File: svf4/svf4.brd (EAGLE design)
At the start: 58.4 x 216.8 mm, 79 parts, among them IC1 OPA4130P, IC2 OPA2134P, Q1 BC550B, Q10 2N3906, Q2 BC550B, Q3 2N3904, Q4 2N3904, Q5 2N3904, Q6 2N3904, Q7 2N3906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

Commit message: finished the rough draft of the state variable board
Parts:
- removed Q10, Q7, Q8, Q9: 2N3906, dan:TO92
- removed Q3, Q4, Q5, Q6: 2N3904, dan:TO92
- removed SV5, SV6: (no value), dan:MA04-1
- added C4, C5, C6: 4.7u, dan:E2,5-6
- added JP1, JP2: (no value), dan:1X06
- added R32: 10k, dan:0207/2V
- added R33: 4.7k, dan:0207/2V
- added R34, R36: 1k, dan:0207/2V
- added R35: 100k, dan:0207/2V
- added U$1, U$2, U$3, U$4: 2N3904_, dan:TO92-EBC
- added U$5, U$6, U$7, U$8: 2N3906_, dan:TO92-EBC
- IC2: value OPA2134P -> OPA4130P; device dan:DIL08 -> dan:DIL14
- R20: value 220k -> 1k
- R27: value 1k -> 4.7k
- R28: value 1k -> 3.3k
- R29: value 1k -> 100k
- R3: value 100k -> 82k
- R30, R31: value 10k -> 100k
- moved R31 142.5 mm to (35.6, 11.4), turned to 270 degrees
- moved R30 141.2 mm to (30.5, 12.7), turned to 180 degrees
- moved R20 76.4 mm to (45.1, 71.8)
- moved R2 56.6 mm to (48.9, 50.2), turned to 90 degrees
- moved R27 44.1 mm to (43.2, 113.0)
- moved R28 41.7 mm to (39.4, 113.0)
- moved D2 38.2 mm to (10.8, 25.4), turned to 90 degrees
- moved R24 37.0 mm to (44.5, 19.1), turned to 180 degrees
- moved R4 36.2 mm to (47.6, 34.3), turned to 270 degrees
- moved R15 35.6 mm to (16.5, 16.5), turned to 0 degrees
- moved R3 35.4 mm to (38.7, 11.4)
- moved D1 33.9 mm to (43.2, 31.8), turned to 90 degrees
- moved R13 31.2 mm to (14.0, 27.9), turned to 270 degrees
- moved RIN1 29.2 mm to (43.8, 171.4)
- moved RIN2 29.2 mm to (14.6, 171.4)
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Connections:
- new net N$38: BPOUT.P$3, R34.2, R35.1
- new net N$41: IC2.14, R32.2, SV7.4
- new net N$42: IC2.13, R32.1, R33.2
- new net N$43: C6.-, R27.1
- new net N$44: C5.+, R26.1
- new net N$45: C4.-, R34.1
- new net N$46: JP2.4, R31.2
- new net N$47: IC2.5, R20.1
- new net N$48: IC2.6, R36.2
- net +12V: now also IC2.4; no longer IC2.8
- net -12V: now also IC2.11; no longer IC2.4
- net -1V: now also IC2.10; no longer IC2.5
- net BP: now also JP2.6; no longer SV5.1
- net GND: now also JP1.2, JP1.5, JP2.2, JP2.5, R20.2, R33.1, R35.2, U$2.B, U$4.B; no longer Q4.2, Q6.2, SV5.2, SV6.2
- net HP: now also IC2.12; no longer SV7.4
- net IN: now also IC1.2, R24.2, R30.1, R31.1, R5.2, R6.2; no longer R20.2, SV5.3
- net N$1: now also U$3.C, U$4.C; no longer Q5.3, Q6.3
- net N$10: now also U$4.E, U$8.E; no longer Q10.1, Q6.1
- net N$14: now also U$3.E, U$7.B, U$7.E, U$8.B; no longer Q10.2, Q5.1, Q9.1, Q9.2
- net N$15: now also U$3.B; no longer Q5.2
- net N$16: now also JP2.1; no longer SV5.4
- net N$17: now also U$7.C, U$8.C; no longer Q10.3, Q9.3
- net N$2: now also U$2.E, U$6.E; no longer Q4.1, Q8.1
- net N$26: now also IC2.8; no longer IC2.7
- net N$28: now also IC2.9; no longer IC2.6
- net N$3: now also U$5.C, U$6.C; no longer Q7.3, Q8.3
- net N$30: now also JP1.1; no longer SV6.4
- net N$32: now also C5.-; no longer R26.1
- net N$33: now also JP1.4; no longer R30.2
- net N$36: now also C4.+, JP1.6; no longer BPOUT.P$3, SV6.1
- net N$37: now also JP2.3, R30.2; no longer R30.1, R31.1, SV6.3
- net N$4: now also U$1.E, U$5.B, U$5.E, U$6.B; no longer Q3.1, Q7.1, Q7.2, Q8.2
- net N$40: now also JP1.3; no longer R31.2
- net N$5: now also U$1.C, U$2.C; no longer Q3.3, Q4.3
- net N$6: now also U$1.B; no longer Q3.2
- net N$7: now also IC2.7, R36.1; no longer IC1.2, R20.1, R24.2, R5.2, R6.2
- net N$8: now also C6.+; no longer R27.1
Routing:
- net +12V: track 0.00 -> 253.6 mm, vias 0 -> 5
- net -12V: track 0.00 -> 195.6 mm, vias 0 -> 5
- net BP: track 0.00 -> 187.8 mm, vias 0 -> 4
- net N$9: track 0.00 -> 151.7 mm, vias 0 -> 3
- net HP: track 0.00 -> 87.2 mm, vias 0 -> 1
- net N$30: track 0.00 -> 81.2 mm, vias 0 -> 1
- net N$33: track 0.00 -> 80.7 mm
- net N$21: track 0.00 -> 80.3 mm, vias 0 -> 3
- net LP: track 0.00 -> 78.3 mm, vias 0 -> 3
- net N$41: track 0.00 -> 72.7 mm, vias 0 -> 1
- net FCIN: track 0.00 -> 64.2 mm
- net N$6: track 0.00 -> 57.0 mm, vias 0 -> 1
- net -1V: track 0.00 -> 56.2 mm, vias 0 -> 2
- net N$25: track 0.00 -> 55.8 mm, vias 0 -> 1
- net N$31: track 0.00 -> 55.4 mm
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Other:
- board size 58.4 x 216.8 mm -> 10.6 x 2.1 mm
- board text added: "-12V"
- board text added: "BP"
- board text added: "HP"
- board text added: "In1"
- board text added: "In2"
- board text added: "LP"
- board text added: "Q1"
- board text added: "Q2"
- board text added: "Q3"
- board text added: "Q4"
- board text added: "Q5"
- board text added: "Q6"
- board text added: "Q7"
- board text added: "Q8"
- board text added: "cv"

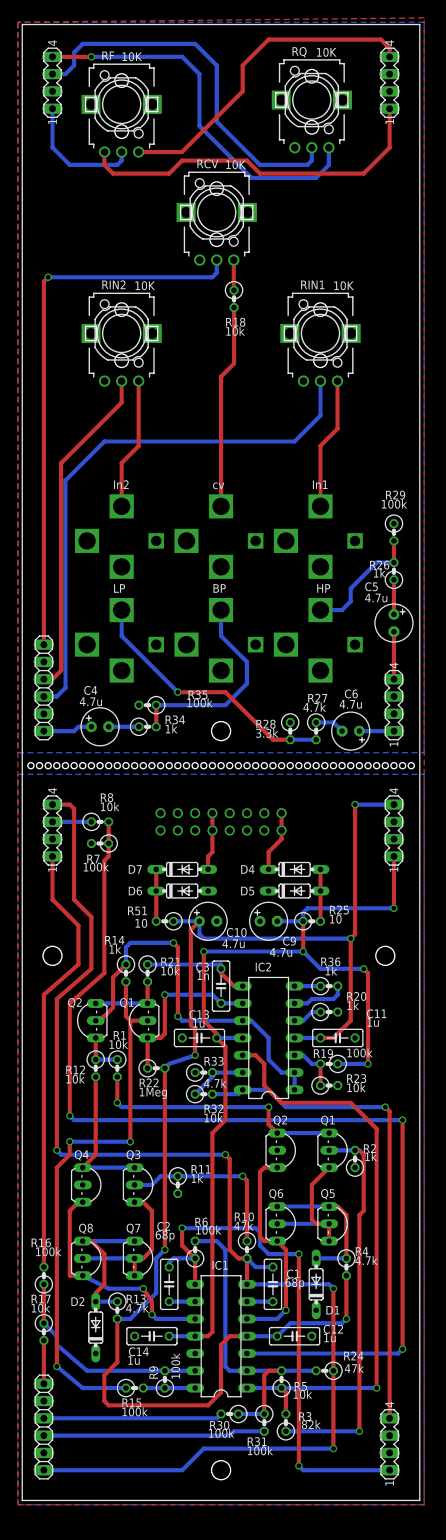
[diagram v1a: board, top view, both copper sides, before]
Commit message: fixed placement of knobs and jacks on svf
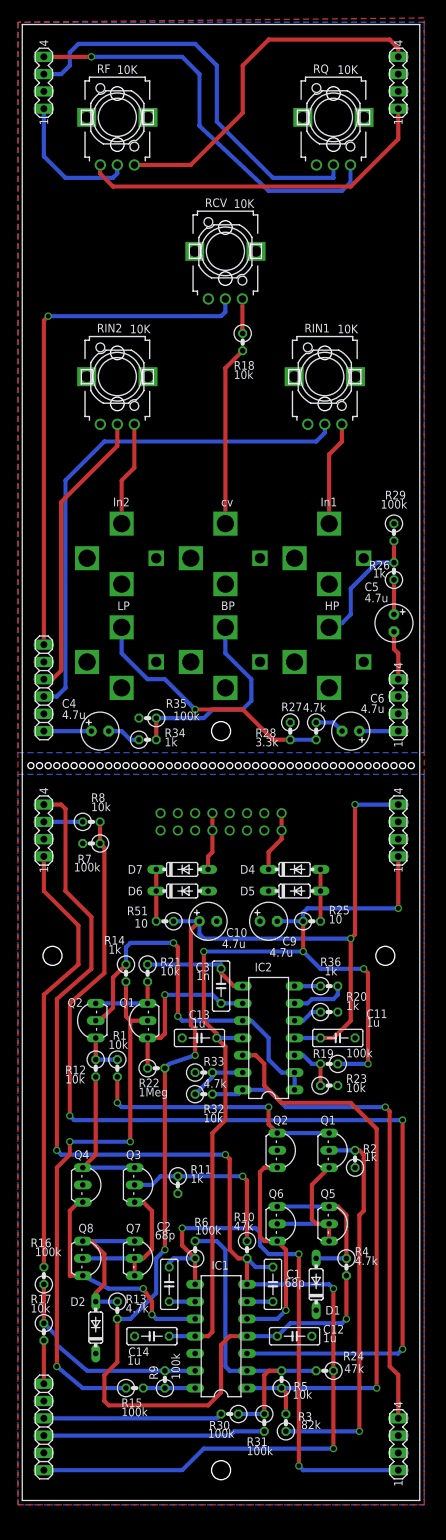
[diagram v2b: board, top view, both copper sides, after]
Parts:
- moved R18 6.48 mm to (32.4, 170.2)
- moved RIN1 6.38 mm to (44.5, 165.1)
- moved RIN2 6.38 mm to (14.0, 165.1)
- moved RCV 5.85 mm to (29.8, 183.5)
- moved RQ 4.07 mm to (45.7, 203.2)
- moved HPOUT 2.84 mm to (45.1, 123.2)
- moved IN 2.84 mm to (45.1, 138.4)
- moved BPOUT 2.62 mm to (29.8, 123.2)
- moved CVIN 2.62 mm to (29.8, 138.4)
- moved LPOUT 2.54 mm to (14.6, 123.2)
- moved IN1 2.54 mm to (14.6, 138.4)
- moved RF 2.01 mm to (14.0, 203.2)
- moved R34 1.91 mm to (18.4, 111.8)
- moved R35 1.91 mm to (18.4, 114.9)
- moved SV3 1.27 mm to (3.17, 98.4)
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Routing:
- net N$40: track 49.3 -> 42.7 mm
- net +12V: track 253.6 -> 258.8 mm
- net N$31: track 55.4 -> 60.4 mm
- net N$25: track 55.8 -> 60.6 mm
- net N$30: track 81.2 -> 76.7 mm
- net N$33: track 80.7 -> 76.4 mm
- net N$34: track 19.4 -> 15.4 mm
- net N$39: track 19.4 -> 15.4 mm
- net N$23: track 30.0 -> 26.5 mm
- net N$19: track 18.4 -> 20.6 mm
- net -12V: track 195.6 -> 197.4 mm
- net LP: track 78.3 -> 79.6 mm
- net LPOUT: track 38.7 -> 37.6 mm
- net N$35: track 18.0 -> 18.7 mm
- net N$8: track 5.08 -> 5.71 mm
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
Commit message: made post fab component changes to 3320 and some fixes to svf board
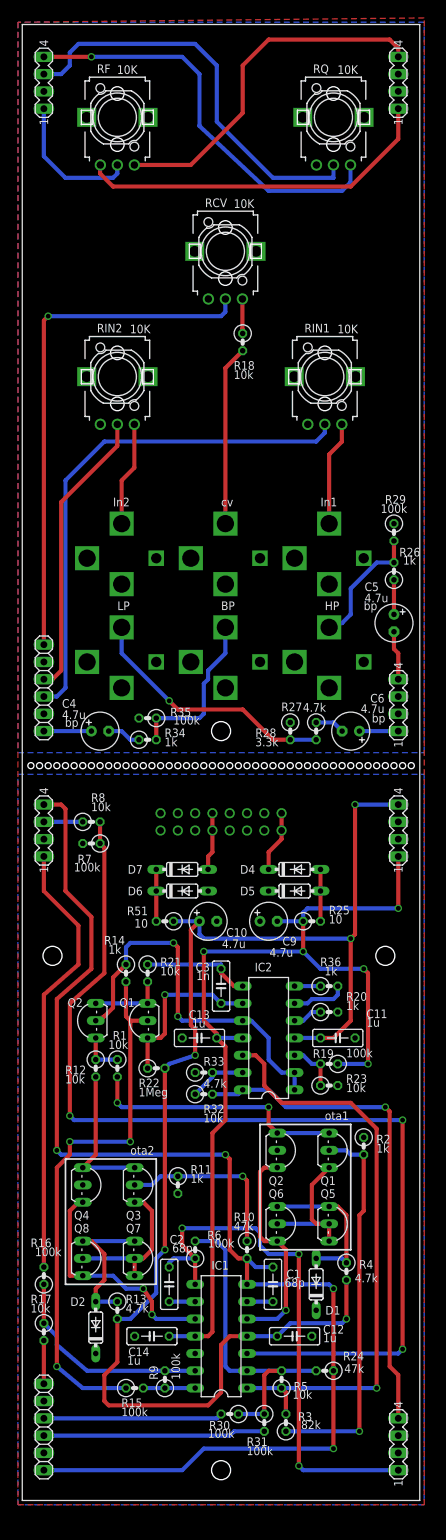
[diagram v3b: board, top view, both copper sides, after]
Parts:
- moved R2 2.29 mm to (50.2, 52.1), turned to 270 degrees
- moved R4 0.63 mm to (47.6, 33.7)
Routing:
- net N$38: track 30.6 -> 24.4 mm
- net N$3: track 21.5 -> 22.4 mm
- net +12V: track 258.8 -> 258.1 mm
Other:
- board text added: "bp"
- board text added: "ota1"
- board text added: "ota2"

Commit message: sent svf to fab.  fixed some significatn errors
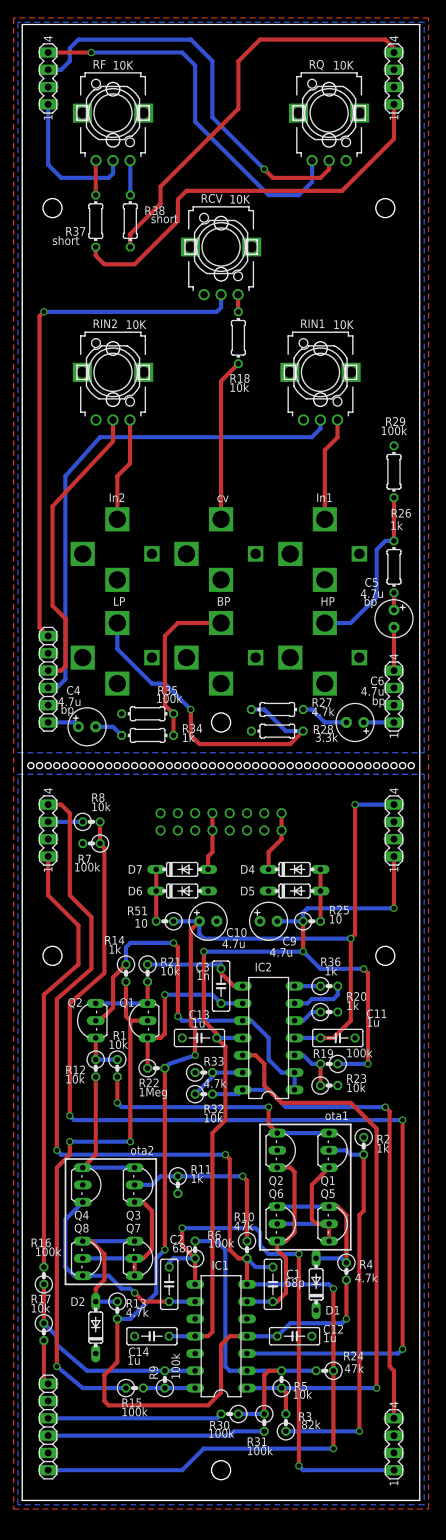
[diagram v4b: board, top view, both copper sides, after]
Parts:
- added R37, R38: short, dan:0204/7
- R18, R26, R27, R28, R29, R34, R35: device dan:0207/2V -> dan:0204/7
- moved R29 8.89 mm to (54.6, 151.1)
- moved R27 6.54 mm to (37.5, 116.2), turned to 180 degrees
- moved C4 2.01 mm to (9.53, 113.7)
- moved R28 1.90 mm to (37.5, 113.0), turned to 0 degrees
- moved JP1 1.42 mm to (3.81, 120.7)
- moved C6 1.42 mm to (48.9, 114.3)
- moved SV8 1.42 mm to (54.6, 118.1)
- moved RIN1 0.90 mm to (43.8, 165.7)
- moved RF 0.90 mm to (13.3, 203.8)
- moved RIN2 0.90 mm to (13.3, 165.7)
- moved RCV 0.90 mm to (29.2, 184.2)
- moved RQ 0.90 mm to (45.1, 203.8)
- moved LPOUT 0.90 mm to (14.0, 123.8)
- moved BPOUT 0.90 mm to (29.2, 123.8)
- moved HPOUT 0.90 mm to (44.5, 123.8)
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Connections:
- removed net N$10: IC1.10, U$4.E, U$8.E
- removed net N$2: IC1.5, U$2.E, U$6.E
- new net N$49: R38.2, RF.3
- new net N$50: R37.1, RF.1
- net +12V: now also R38.1; no longer RF.3
- net -12V: now also R37.2; no longer RF.1
- net GND: now also IC1.10, IC1.5, RQ.3; no longer RQ.1
- net N$11: now also U$2.E, U$6.E
- net N$18: now also U$4.E, U$8.E
- net N$25: now also RQ.1; no longer RQ.3
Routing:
- net N$10: track 34.3 -> 0.00 mm, vias 2 -> 0
- net N$2: track 32.1 -> 0.00 mm, vias 1 -> 0
- net N$18: track 3.81 -> 31.7 mm, vias 0 -> 1
- net N$11: track 3.81 -> 29.1 mm
- net LPOUT: track 37.6 -> 48.9 mm
- net N$35: track 18.7 -> 25.6 mm
- net +12V: track 258.1 -> 264.4 mm
- net -12V: track 197.4 -> 202.6 mm
- net N$50: track 0.00 -> 5.08 mm
- net N$49: track 0.00 -> 5.08 mm
- net N$25: track 60.6 -> 56.2 mm
- net N$43: track 4.34 -> 7.14 mm
- net N$23: track 26.5 -> 23.9 mm
- net N$44: track 5.08 -> 2.54 mm
- net CV: track 5.07 -> 2.53 mm
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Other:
- board size 10.6 x 2.1 mm -> 58.4 x 216.8 mm

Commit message: respun the svf.  changed a few components on the 3320
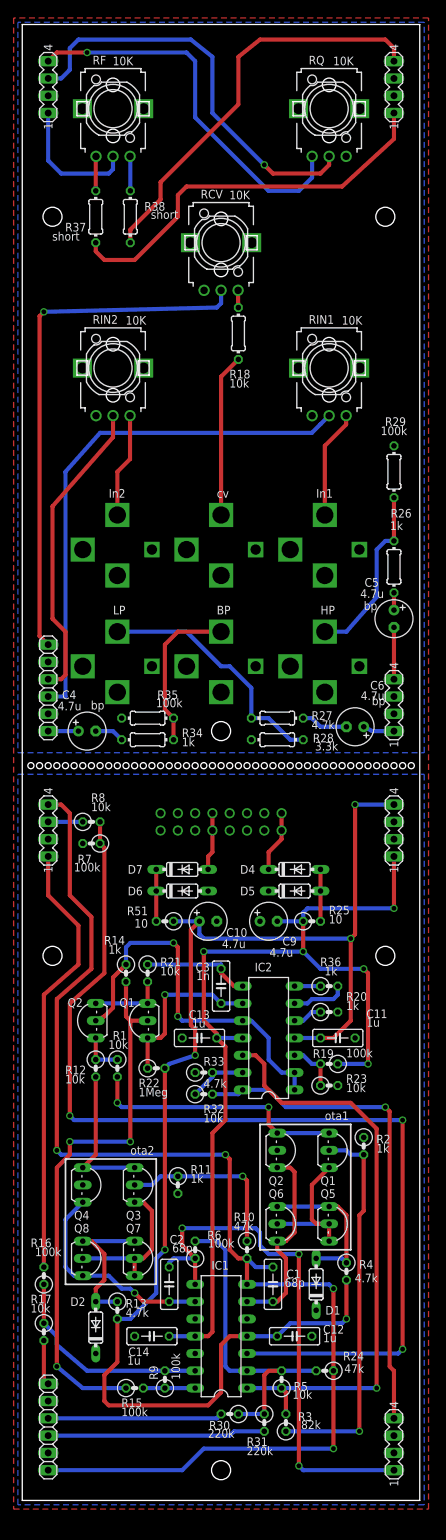
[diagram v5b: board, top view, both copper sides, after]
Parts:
- R30, R31: value 100k -> 220k
- moved RIN1 1.42 mm to (45.1, 166.4)
- moved JP1 1.27 mm to (3.81, 119.4)
- moved BPOUT 1.27 mm to (29.2, 122.6)
- moved HPOUT 1.27 mm to (44.5, 122.6)
- moved LPOUT 1.27 mm to (14.0, 122.6)
- moved R27 1.27 mm to (37.5, 114.9)
- moved R28 1.27 mm to (37.5, 111.8)
- moved SV8 1.27 mm to (54.6, 116.8)
- moved SV2 1.27 mm to (54.6, 207.6)
- moved SV4 1.27 mm to (3.81, 207.6)
- moved C4 0.64 mm to (9.53, 113.0)
- moved C6 0.63 mm to (48.9, 113.7)
- moved CVIN 0.63 mm to (29.2, 139.7)
- moved IN 0.63 mm to (44.5, 139.7)
- moved IN1 0.63 mm to (14.0, 139.7)
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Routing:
- net LPOUT: track 48.9 -> 36.5 mm, vias 1 -> 0
- net N$33: track 74.7 -> 77.9 mm
- net N$19: track 21.4 -> 19.5 mm
- net N$40: track 43.3 -> 45.0 mm
- net -12V: track 202.6 -> 200.8 mm
- net N$30: track 76.6 -> 77.9 mm
- net N$32: track 6.35 -> 7.62 mm
- net N$31: track 59.3 -> 60.1 mm
- net +12V: track 264.4 -> 265.3 mm
- net N$35: track 25.6 -> 26.3 mm
- net N$38: track 24.2 -> 23.5 mm
- net N$34: track 15.4 -> 15.9 mm

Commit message: updated svf with dc offset trim pots and transistors for biasing
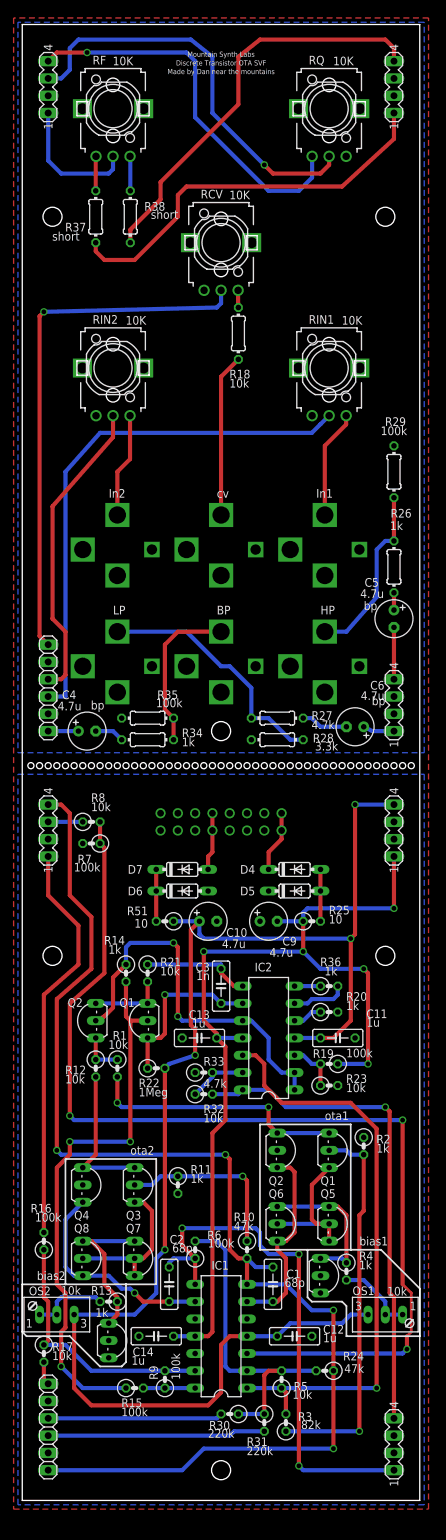
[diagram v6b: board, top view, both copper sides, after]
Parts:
- removed D1, D2: 1N4148DO35-7, dan:DO35-7
- added OS1, OS2: 10k, dan:S64W
- added U$10, U$9: 2N3906_, dan:TO92-EBC
- R13, R4: value 4.7k -> 1k
- moved R16 5.08 mm to (3.17, 38.1)
- moved R17 3.18 mm to (3.17, 21.6)
- moved R13 1.80 mm to (12.7, 29.2), turned to 180 degrees
- moved C14 0.63 mm to (19.7, 24.1)
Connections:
- new net N$10: OS2.A, OS2.S, R13.2
- new net N$2: OS1.A, OS1.S, R4.2
- net +12V: now also OS1.E, OS2.E; no longer R13.2, R4.2
- net GND: now also U$10.B, U$10.E, U$9.B, U$9.E; no longer D1.C, D2.C
- net N$17: now also U$10.C; no longer D2.A
- net N$3: now also U$9.C; no longer D1.A
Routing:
- net N$2: track 0.00 -> 11.5 mm
- net N$10: track 0.00 -> 11.3 mm
- net +12V: track 265.3 -> 272.3 mm, vias 5 -> 4
- net N$13: track 31.4 -> 38.3 mm
- net FCIN: track 64.5 -> 59.4 mm
- net N$16: track 6.61 -> 3.44 mm
- net BP: track 187.0 -> 185.1 mm
- net N$9: track 151.7 -> 153.1 mm
- net N$17: track 22.3 -> 23.1 mm
- net -12V: track 200.8 -> 200.2 mm
- net N$3: track 22.4 -> 21.7 mm
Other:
- board text added: "Discrete Transistor OTA SVF"
- board text added: "Made by Dan near the mountains"
- board text added: "Mountain Synth Labs"
- board text added: "bias1"
- board text added: "bias2"
